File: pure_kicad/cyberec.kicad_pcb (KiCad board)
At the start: 4 copper layers, 50 x 50 mm, 142 parts, among them J1 XT30M, J2 XT30F, J3 XT60M, J4 XT60M, J5 Conn_01x04_Pin, J6 Conn_01x04_Pin, Q1 Q_NMOS_DGS, Q2 Q_NMOS_DGS, Q3 Q_NMOS_DGS, Q4 Q_NMOS_DGS, Q5 Q_PMOS_SGD, Q6 Q_NMOS_DGS, Q7 Q_NMOS_DGS, U1 BQ25756ERRVR, U2 BQ40Z80RSMR

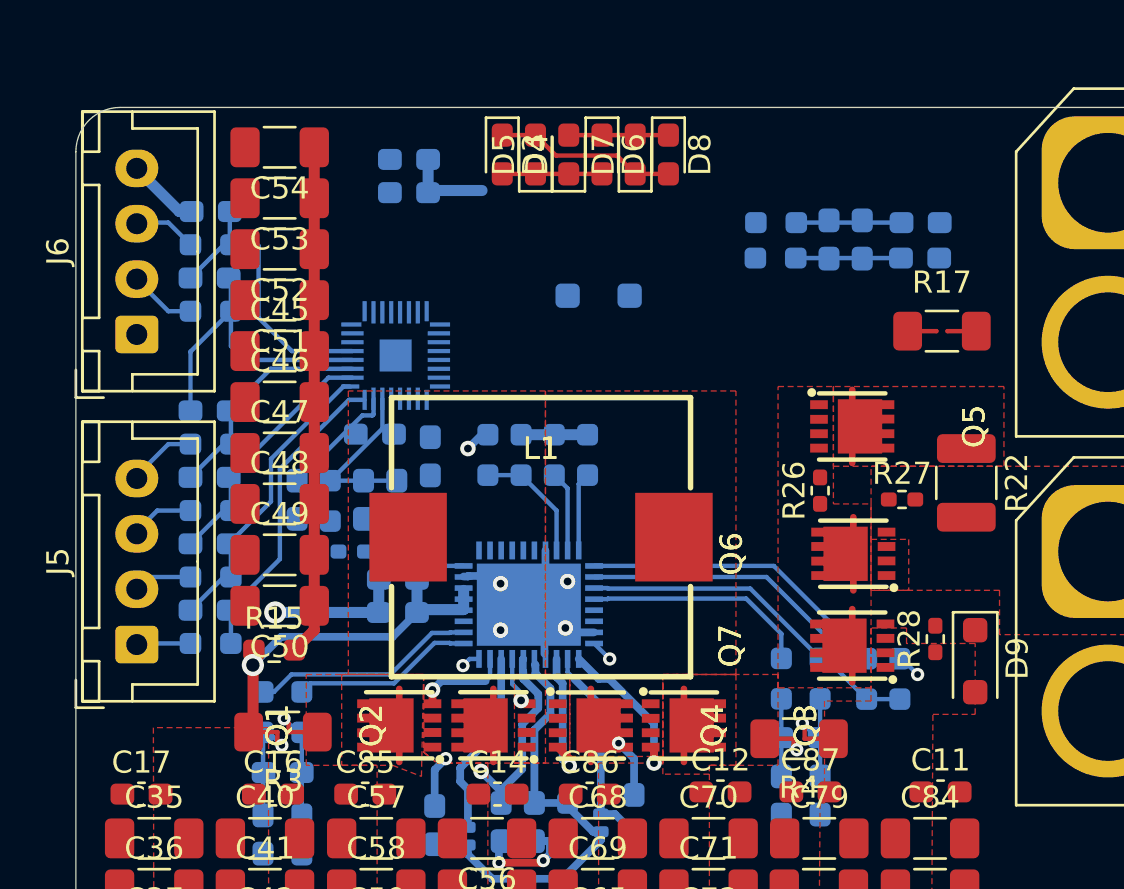
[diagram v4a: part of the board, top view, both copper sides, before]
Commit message: Layout is mostly good. Still need i2c and stuff
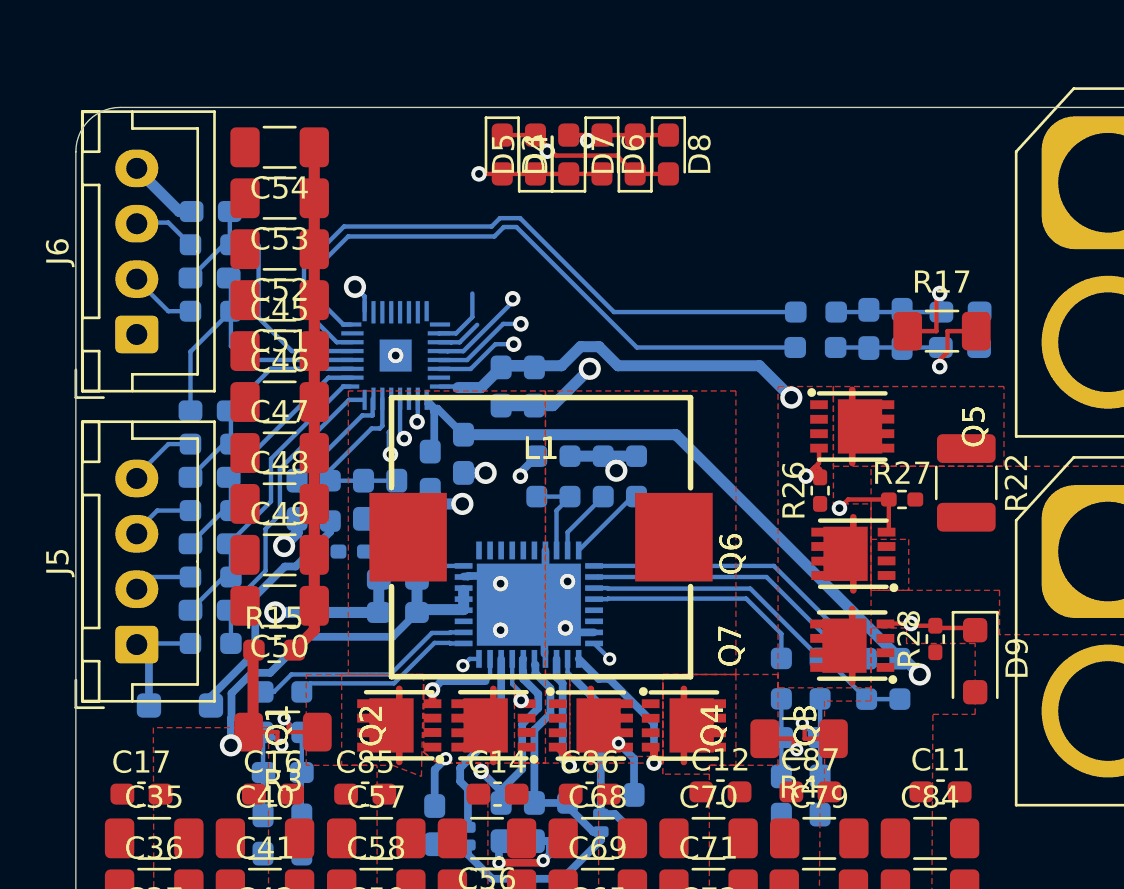
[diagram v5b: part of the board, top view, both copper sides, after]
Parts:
- D10, D9: footprint Diode_SMD:D_SOD-123F -> cyberec:D_SOD-123F
- moved D10 26.4 mm to (79.7, 102.0)
- moved C30 11.7 mm to (95.7, 87.6), turned to 90 degrees
- moved C29 9.69 mm to (94.2, 87.6), turned to 90 degrees
- moved C19 4.42 mm to (114.9, 85.8)
- moved R16 4.42 mm to (108.4, 85.8)
- moved C20 4.42 mm to (112.3, 85.0)
- moved C21 4.42 mm to (110.8, 85.0)
- moved C22 4.42 mm to (114.9, 84.2)
- moved R18 4.42 mm to (108.4, 84.2)
- moved C34 3.00 mm to (91.0, 91.4), turned to -90 degrees
- moved R10 2.41 mm to (97.3, 91.7)
- moved R7 2.41 mm to (98.8, 91.7)
- moved R8 2.41 mm to (100.3, 91.7)
- moved R9 2.41 mm to (95.8, 91.7)
- moved C13 1.50 mm to (92.5, 90.6)
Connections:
- net Net-(J5-Pin_2) renamed /Battery Monitor/cell5
- net Net-(J5-Pin_3) renamed /Battery Monitor/cell4
- net Net-(J5-Pin_4) renamed /Battery Monitor/cell3
- net Net-(J6-Pin_2) renamed /Battery Monitor/cell2
- net Net-(J6-Pin_3) renamed /Battery Monitor/cell1
- D10 pad 2: +BATT -> /Battery Monitor/cell6
- J5 pad 1: Net-(J5-Pin_1) -> /Battery Monitor/cell6
- R19 pad 2: Net-(J5-Pin_1) -> /Battery Monitor/cell6
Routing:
- net /Battery Monitor/DSG: track 0.00 -> 33.0 mm, vias 0 -> 2
- net /Battery Monitor/SRN: track 0.00 -> 29.6 mm
- net VCC: track 1.10 -> 30.1 mm
- net Net-(J3-Pin_2): track 0.00 -> 28.9 mm
- net /Battery Monitor/SRP: track 0.00 -> 28.2 mm
- net /Battery Monitor/CHG: track 0.00 -> 28.1 mm, vias 0 -> 2
- net /Battery Monitor/PCHG: track 0.00 -> 23.7 mm, vias 0 -> 2
- net /Battery Monitor/LED_C: track 4.50 -> 20.4 mm, vias 0 -> 2
- net VDDF: track 3.98 -> 19.2 mm, vias 0 -> 1
- net /Battery Monitor/LED_A: track 8.22 -> 22.1 mm, vias 0 -> 2
- net /Battery Monitor/LED_B: track 4.50 -> 18.3 mm, vias 0 -> 2
- net -BATT: track 3.38 -> 16.1 mm, vias 0 -> 5
- net Net-(D10-K): track 0.00 -> 10.8 mm
- net /Battery Monitor/cell6: track 0.00 -> 5.48 mm
- net VAC: track 16.7 -> 20.6 mm
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- added copper zone on In2.Cu, net -BATT

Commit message: I think this was just sorting LEDs
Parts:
- moved R6 2.05 mm to (107.0, 99.5), turned to -45 degrees
- moved D5 1.71 mm to (97.5, 77.3)
- moved R11 1.53 mm to (113.5, 100.0)
- moved D4 1.32 mm to (96.0, 77.4)
- moved R12 1.32 mm to (112.0, 101.0)
- moved R2 1.00 mm to (105.9, 100.8), turned to -45 degrees
- moved D6 0.35 mm to (99.0, 77.4)
- moved D7 0.35 mm to (100.5, 77.4)
- moved D8 0.35 mm to (102.0, 77.4)
- moved D3 0.32 mm to (94.5, 77.4)
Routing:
- net VCC: track 30.1 -> 34.6 mm
- net /Charger/FB: track 16.7 -> 19.6 mm
- net /Battery Monitor/LED_C: track 20.4 -> 23.3 mm
- net /Charger/SRN: track 11.5 -> 8.85 mm
- net /Charger/FBG: track 14.0 -> 16.4 mm
- net /Battery Monitor/LED_A: track 22.1 -> 24.1 mm
- net /Charger/SRP: track 10.2 -> 8.60 mm
- net Net-(C4-Pad2): track 5.29 -> 6.52 mm
- net Net-(C2-Pad2): track 4.97 -> 6.20 mm
- net /Charger/BTST1: track 10.3 -> 11.4 mm
- net /Charger/REGN: track 24.6 -> 25.6 mm
- net /Charger/SW1: track 3.19 -> 2.94 mm, vias 2 -> 6
- net VDDF: vias 1 -> 10
- net VDDA: vias 0 -> 6
- net VDD: vias 0 -> 6
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
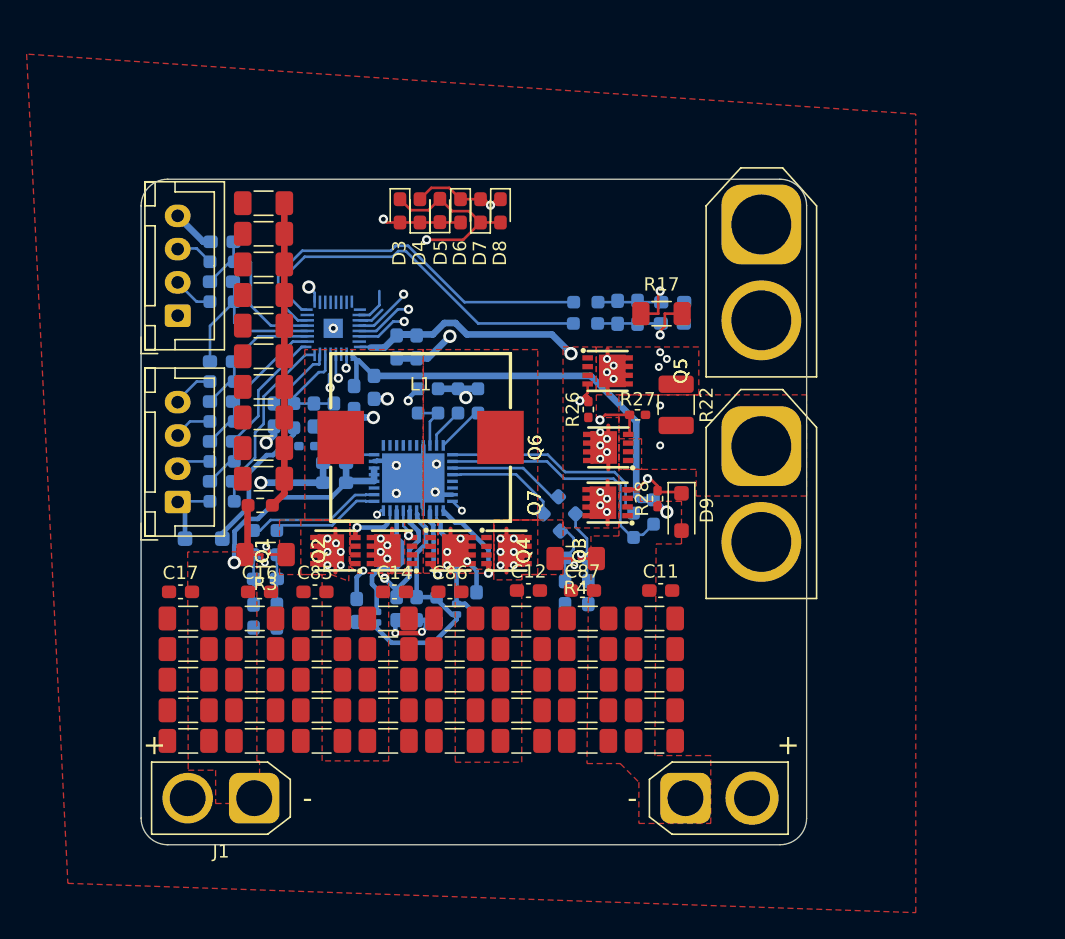
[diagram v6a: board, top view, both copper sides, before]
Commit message: Re-layout top side. Bottom to follow
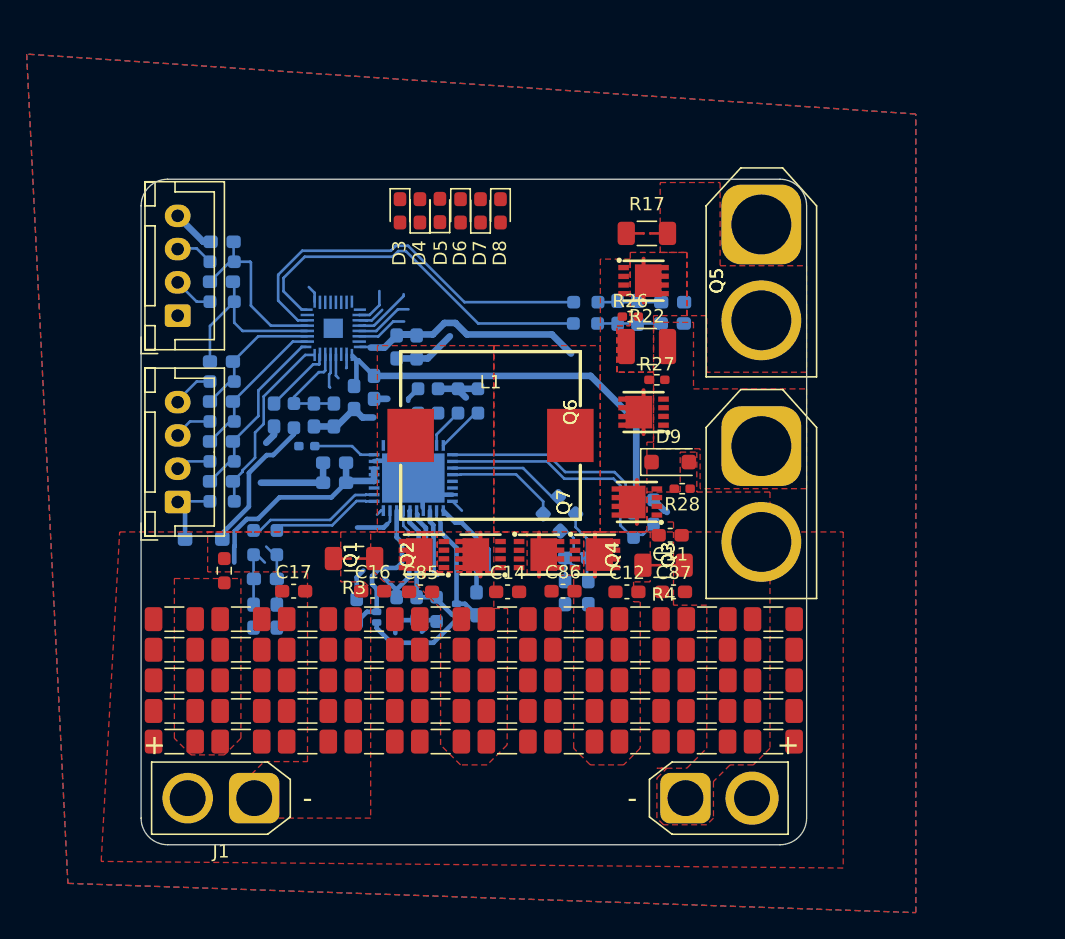
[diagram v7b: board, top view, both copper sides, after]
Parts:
- moved C45 32.0 mm to (77.5, 117.2)
- moved C51 32.0 mm to (77.5, 115.0)
- moved C52 32.0 mm to (77.5, 112.7)
- moved C53 32.0 mm to (77.5, 110.3)
- moved C54 32.0 mm to (77.5, 108.0)
- moved C46 29.0 mm to (82.5, 117.2), turned to 180 degrees
- moved C47 24.4 mm to (82.5, 115.0), turned to 180 degrees
- moved C48 19.8 mm to (82.5, 112.7), turned to 180 degrees
- moved C49 15.2 mm to (82.5, 110.3), turned to 180 degrees
- moved C50 10.7 mm to (82.5, 108.0), turned to 0 degrees
- moved C35 8.96 mm to (87.5, 108.0)
- moved C36 8.96 mm to (87.5, 110.3)
- moved C37 8.96 mm to (87.5, 112.7)
- moved C38 8.96 mm to (87.5, 115.0)
- moved C39 8.96 mm to (87.5, 117.2)
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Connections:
- net Net-(C45-Pad2) renamed /Charger/VAC_DAMP
- net Net-(J3-Pin_2) renamed /Battery Monitor/BATT_JOIN
- net Net-(Q5-D) renamed /Battery Monitor/PCHG_R
- C34 pad 1: VCC -> -BATT
- C34 pad 2: -BATT -> VCC
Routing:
- net /Charger/VAC_DAMP: track 23.1 -> 0.00 mm
- net /Battery Monitor/LED_A: track 24.1 -> 10.5 mm, vias 2 -> 0
- net /Battery Monitor/LED_C: track 23.3 -> 16.2 mm, vias 2 -> 0
- net /Battery Monitor/LED_B: track 18.7 -> 12.8 mm, vias 2 -> 0
- net /Battery Monitor/DSG: track 33.2 -> 28.2 mm, vias 2 -> 0
- net /Battery Monitor/CHG: track 28.1 -> 24.2 mm, vias 2 -> 0
- net VAC: track 20.6 -> 16.8 mm, vias 1 -> 0
- net /Battery Monitor/PCHG: track 23.7 -> 21.0 mm, vias 2 -> 0
- net Earth: track 31.0 -> 29.0 mm, vias 9 -> 0
- net Net-(C20-Pad2): track 7.38 -> 5.62 mm, vias 1 -> 0
- net Net-(C19-Pad2): track 7.38 -> 5.63 mm, vias 1 -> 0
- net /Charger/LODRV2: track 6.13 -> 5.06 mm, vias 1 -> 0
- net /Charger/HIDRV1: track 4.28 -> 3.47 mm, vias 1 -> 0
- net /Charger/HIDRV2: track 7.17 -> 6.39 mm, vias 1 -> 0
- net Net-(C3-Pad2): track 5.49 -> 4.80 mm, vias 1 -> 0
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- added copper zone on F.Cu, net -BATT
- added copper zone on F.Cu, net /Charger/VAC_DAMP
- added copper zone on B.Cu, net Earth

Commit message: Most of the layout/routing on the back side
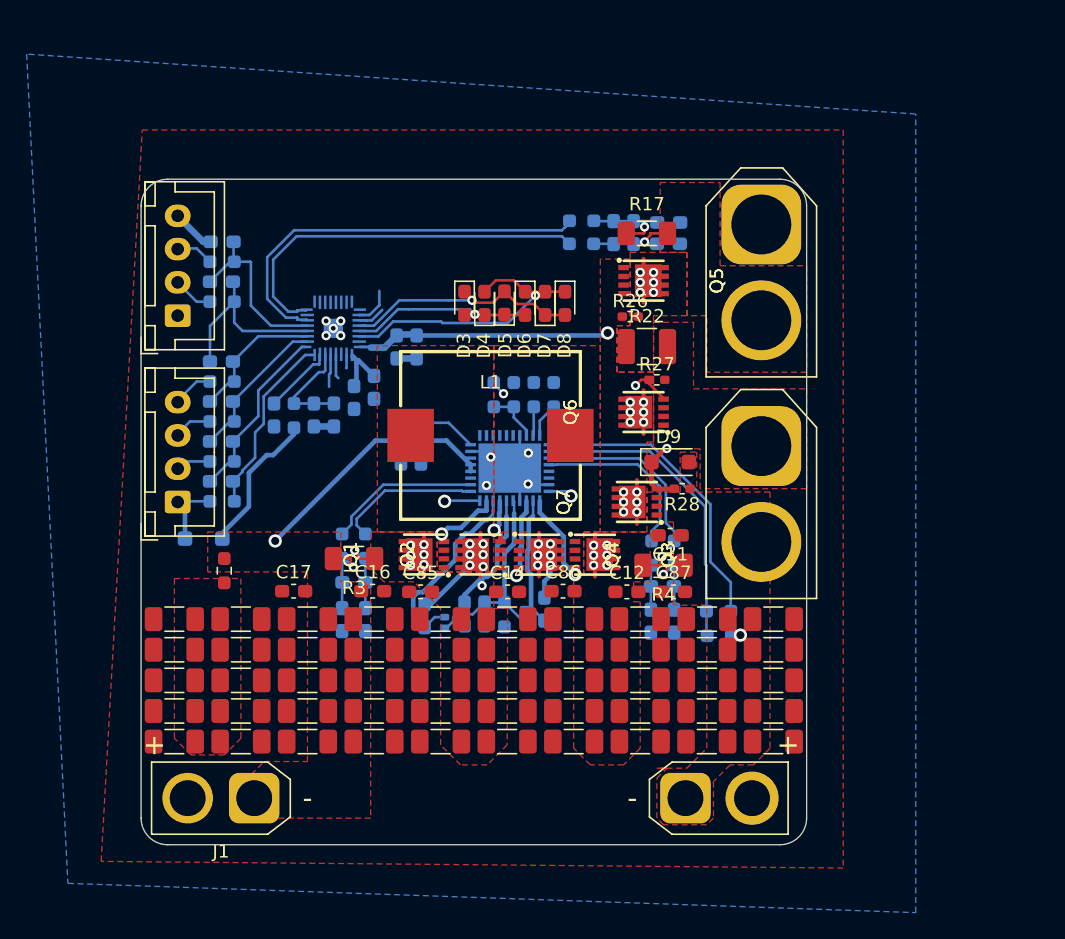
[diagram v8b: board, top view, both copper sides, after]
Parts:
- moved R11 10.5 mm to (118.4, 109.3), turned to 180 degrees
- moved R12 9.08 mm to (118.4, 107.5), turned to 0 degrees
- moved R6 8.81 mm to (115.0, 103.1), turned to -90 degrees
- moved D3 8.47 mm to (99.3, 84.3)
- moved D4 8.47 mm to (100.8, 84.3)
- moved D5 8.47 mm to (102.3, 84.3)
- moved D6 8.47 mm to (103.8, 84.3)
- moved D7 8.47 mm to (105.3, 84.3)
- moved D8 8.47 mm to (106.8, 84.3)
- moved R14 8.38 mm to (95.7, 93.3)
- moved R2 7.84 mm to (113.3, 103.1), turned to -90 degrees
- moved U1 7.29 mm to (102.7, 96.7)
- moved C15 6.88 mm to (96.0, 95.5), turned to -90 degrees
- moved C2 6.79 mm to (113.3, 108.2)
- moved C6 6.79 mm to (115.0, 108.2)
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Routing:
- net VCC: track 34.6 -> 5.75 mm, vias 0 -> 1
- net /Battery Monitor/DSG: track 28.2 -> 6.13 mm, vias 0 -> 1
- net /Battery Monitor/PCHG: track 21.0 -> 1.88 mm
- net /Battery Monitor/CHG: track 24.2 -> 5.58 mm, vias 0 -> 1
- net Earth: track 29.0 -> 12.4 mm, vias 0 -> 4
- net -BATT: track 16.1 -> 6.58 mm, vias 0 -> 5
- net /Battery Monitor/LED_A: track 10.5 -> 18.2 mm, vias 0 -> 1
- net /Charger/FBG: track 16.4 -> 22.6 mm
- net /Charger/SRN: track 8.85 -> 14.1 mm
- net /Battery Monitor/LED_C: track 16.2 -> 21.4 mm, vias 0 -> 1
- net /Charger/SRP: track 8.60 -> 13.4 mm
- net /Charger/SW1: track 2.94 -> 7.29 mm, vias 0 -> 7
- net /Charger/FB: track 19.6 -> 23.2 mm
- net /Charger/BTST1: track 11.4 -> 14.7 mm
- net /Charger/DRV_SUP: track 18.4 -> 15.5 mm
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- added copper zone on In2.Cu, net VCC
